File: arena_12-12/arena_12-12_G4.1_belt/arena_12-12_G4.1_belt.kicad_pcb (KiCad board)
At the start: 2 copper layers, 228.6 x 228.6 mm, 41 parts, among them J4 Barrel_Jack, P1 CONN15, P10 CONN15, P11 CONN15, P12 CONN15, P2 CONN15, P3 CONN15, P4 CONN15, P5 CONN15, P6 CONN15, P7 CONN15, P8 CONN15, P9 CONN15

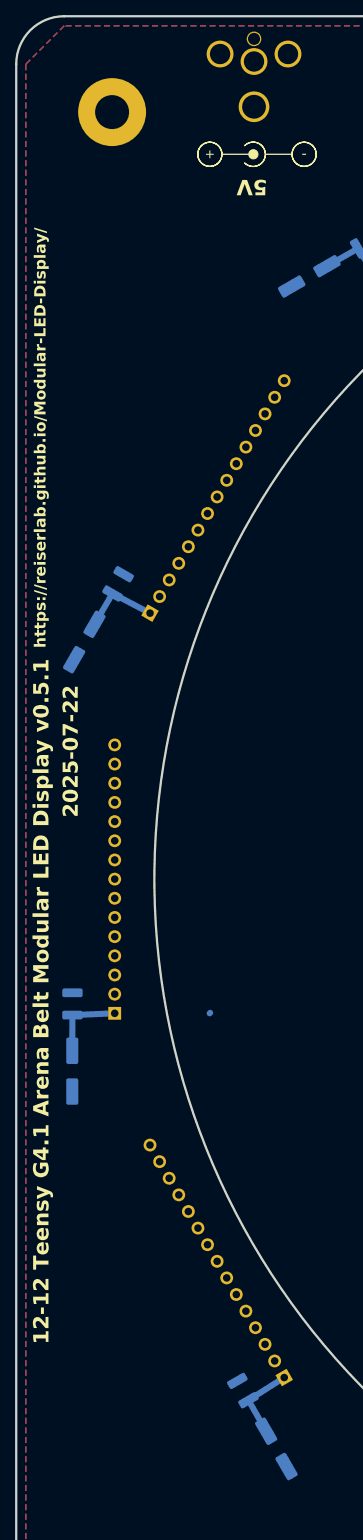
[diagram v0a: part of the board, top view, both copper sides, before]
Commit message: cleanup, belt with SMD power connector
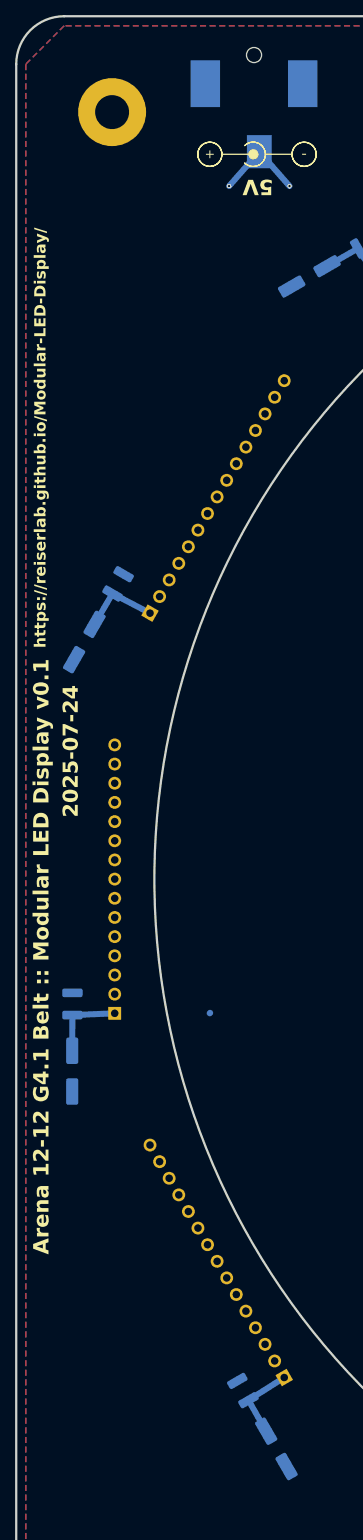
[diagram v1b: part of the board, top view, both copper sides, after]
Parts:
- J4: footprint arena_custom:DCJACK_2PIN_HIGHCURRENT -> Connector_BarrelJack:BarrelJack_CUI_PJ-036AH-SMT_Horizontal
- moved J4 12.1 mm to (95.0, 75.6), turned to 0 degrees
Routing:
- net +5V: track 124.1 -> 136.3 mm, vias 0 -> 2
